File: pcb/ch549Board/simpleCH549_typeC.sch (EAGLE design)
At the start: 14 parts, among them J4 USB_A_SMT_MALE, U2 CH552G

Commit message: update pins in text editor
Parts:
- LED2: value P3.3 -> P2.2
- U2: value CH552G -> CH549G; device myOwnLib:MY_IC_CH551G_CH552GSOP-16 -> myOwnLib:MY_IC_CH549GSOP-16
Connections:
- removed net P3.2: J2.5, U2.P3.2
- removed net P3.3: J2.6, R3.1, U2.P3.3
- new net P2.2: J2.6, R3.1, U2.P2.2
- new net P2.4: J2.7, U2.P2.4
- net P1.1: now also J2.5; no longer J1.2
- net P3.0: now also J2.4; no longer J2.3
- net P3.1: now also J2.3; no longer J2.4
- net P3.4: now also J1.2; no longer J2.7
- net USB_D+: now also U2.P5.1; no longer U2.P3.6
- net USB_D-: now also U2.P5.0; no longer U2.P3.7
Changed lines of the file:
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@@
 <part name="GND3" library="SparkFun-PowerSymbols" library_urn="urn:adsk.eagle:library:530" deviceset="GND" device=""/>
 <part name="R2" library="rcl" library_urn="urn:adsk.eagle:library:334" deviceset="R-US_" device="R0805" package3d_urn="urn:adsk.eagle:package:23553/2" value="20K"/>
-<part name="U2" library="myOwnLib" deviceset="MY_IC_CH551G_CH552G" device="SOP-16" value="CH552G">
+<part name="U2" library="myOwnLib" deviceset="MY_IC_CH549G" device="SOP-16" value="CH549G">
 <attribute name="LCSC" value="C111292"/>
 </part>
@@
 <part name="S1" library="SparkFun-Switches" library_urn="urn:adsk.eagle:library:535" deviceset="MOMENTARY-SWITCH-SPST" device="-SMD-6.2MM-TALL" package3d_urn="urn:adsk.eagle:package:40172/1"/>
 <part name="R3" library="rcl" library_urn="urn:adsk.eagle:library:334" deviceset="R-US_" device="R0805" package3d_urn="urn:adsk.eagle:package:23553/2" value="20K"/>
-<part name="LED2" library="BeagleBone_Black_Wireless" library_urn="urn:adsk.eagle:library:6644236" deviceset="GHI-BASICCOMPONENTS_LED-(INCH)-" device="0805" package3d_urn="urn:adsk.eagle:package:6644356/2" value="P3.3"/>
+<part name="LED2" library="BeagleBone_Black_Wireless" library_urn="urn:adsk.eagle:library:6644236" deviceset="GHI-BASICCOMPONENTS_LED-(INCH)-" device="0805" package3d_urn="urn:adsk.eagle:package:6644356/2" value="P2.2"/>
 <part name="GND6" library="SparkFun-PowerSymbols" library_urn="urn:adsk.eagle:library:530" deviceset="GND" device=""/>
 <part name="GOLD_ORB_SM1" library="oshw" deviceset="OSHWLOGO" device="LOGO8MM"/>
@@
 <wire x1="127" y1="25.4" x2="134.62" y2="25.4" width="0.1524" layer="91"/>
 <label x="127" y="25.4" size="1.778" layer="95"/>
-<pinref part="U2" gate="G$1" pin="P3.7"/>
+<pinref part="U2" gate="G$1" pin="P5.0"/>
 </segment>
 </net>
@@
 <wire x1="127" y1="22.86" x2="134.62" y2="22.86" width="0.1524" layer="91"/>
 <label x="127" y="22.86" size="1.778" layer="95"/>
-<pinref part="U2" gate="G$1" pin="P3.6"/>
+<pinref part="U2" gate="G$1" pin="P5.1"/>
 </segment>
 <segment>
@@
 </segment>
 </net>
-<net name="P1.1" class="0">
+<net name="P3.4" class="0">
 <segment>
 <label x="127" y="30.48" size="1.778" layer="95"/>
 <wire x1="133.35" y1="30.48" x2="127" y2="30.48" width="0.1524" layer="91"/>
-<pinref part="U2" gate="G$1" pin="P1.1"/>
+<pinref part="U2" gate="G$1" pin="P3.4"/>
 </segment>
 <segment>
@@
 </segment>
 </net>
-<net name="P3.4" class="0">
+<net name="P2.4" class="0">
 <segment>
 <wire x1="127" y1="20.32" x2="134.62" y2="20.32" width="0.1524" layer="91"/>
 <label x="127" y="20.32" size="1.778" layer="95"/>
-<pinref part="U2" gate="G$1" pin="P3.4"/>
+<pinref part="U2" gate="G$1" pin="P2.4"/>
 </segment>
 <segment>
@@
 </segment>
 </net>
-<net name="P3.3" class="0">
+<net name="P2.2" class="0">
 <segment>
 <label x="127" y="17.78" size="1.778" layer="95"/>
 <wire x1="127" y1="17.78" x2="134.62" y2="17.78" width="0.1524" layer="91"/>
-<pinref part="U2" gate="G$1" pin="P3.3"/>
+<pinref part="U2" gate="G$1" pin="P2.2"/>
 <pinref part="R3" gate="G$1" pin="1"/>
 </segment>
@@
 </segment>
 </net>
-<net name="P3.2" class="0">
+<net name="P1.1" class="0">
 <segment>
 <wire x1="127" y1="15.24" x2="134.62" y2="15.24" width="0.1524" layer="91"/>
 <label x="127" y="15.24" size="1.778" layer="95"/>
-<pinref part="U2" gate="G$1" pin="P3.2"/>
+<pinref part="U2" gate="G$1" pin="P1.1"/>
 </segment>
 <segment>
@@
 </segment>
 </net>
-<net name="P3.1" class="0">
+<net name="P3.0" class="0">
 <segment>
 <label x="127" y="12.7" size="1.778" layer="95"/>
 <wire x1="127" y1="12.7" x2="134.62" y2="12.7" width="0.1524" layer="91"/>
-<pinref part="U2" gate="G$1" pin="P3.1"/>
+<pinref part="U2" gate="G$1" pin="P3.0"/>
 </segment>
 <segment>
@@
 </segment>
 </net>
-<net name="P3.0" class="0">
+<net name="P3.1" class="0">
 <segment>
 <label x="127" y="10.16" size="1.778" layer="95"/>
 <wire x1="127" y1="10.16" x2="134.62" y2="10.16" width="0.1524" layer="91"/>
-<pinref part="U2" gate="G$1" pin="P3.0"/>
-</segment>
-<segment>
+<pinref part="U2" gate="G$1" pin="P3.1"/>
+</segment>
+<segment>

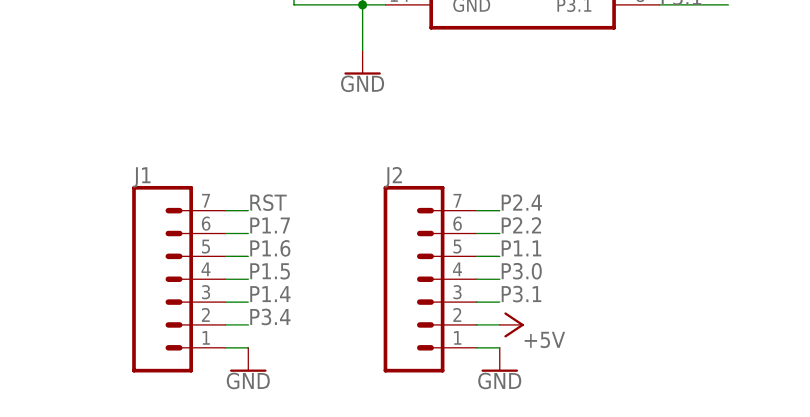
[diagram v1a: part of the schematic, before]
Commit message: adjust pins
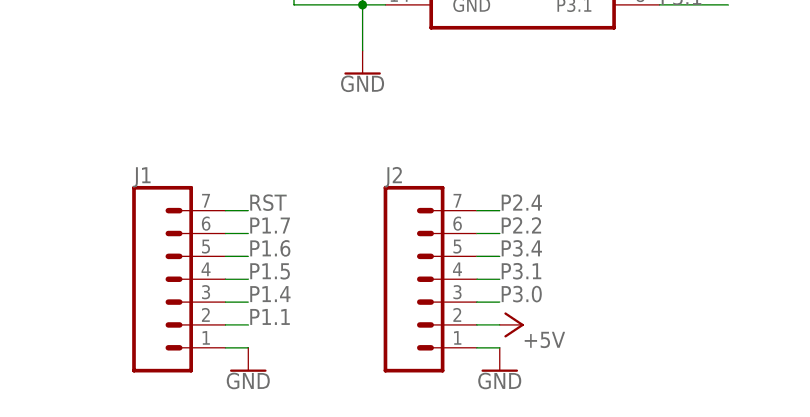
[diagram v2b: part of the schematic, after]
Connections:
- net P1.1: now also J1.2; no longer J2.5
- net P3.0: now also J2.3; no longer J2.4
- net P3.1: now also J2.4; no longer J2.3
- net P3.4: now also J2.5; no longer J1.2
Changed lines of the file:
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@@
 </segment>
 <segment>
-<pinref part="J1" gate="G$1" pin="2"/>
-<wire x1="78.74" y1="-25.4" x2="81.28" y2="-25.4" width="0.1524" layer="91"/>
-<label x="81.28" y="-25.4" size="1.778" layer="95"/>
+<pinref part="J2" gate="G$1" pin="5"/>
+<wire x1="106.68" y1="-17.78" x2="109.22" y2="-17.78" width="0.1524" layer="91"/>
+<label x="109.22" y="-17.78" size="1.778" layer="95"/>
 </segment>
 </net>
@@
 </segment>
 <segment>
-<pinref part="J2" gate="G$1" pin="5"/>
-<wire x1="106.68" y1="-17.78" x2="109.22" y2="-17.78" width="0.1524" layer="91"/>
-<label x="109.22" y="-17.78" size="1.778" layer="95"/>
-</segment>
-</net>
-<net name="P3.0" class="0">
-<segment>
-<label x="127" y="12.7" size="1.778" layer="95"/>
-<wire x1="127" y1="12.7" x2="134.62" y2="12.7" width="0.1524" layer="91"/>
-<pinref part="U2" gate="G$1" pin="P3.0"/>
-</segment>
-<segment>
-<pinref part="J2" gate="G$1" pin="4"/>
-<wire x1="106.68" y1="-20.32" x2="109.22" y2="-20.32" width="0.1524" layer="91"/>
-<label x="109.22" y="-20.32" size="1.778" layer="95"/>
-</segment>
-</net>
-<net name="P3.1" class="0">
-<segment>
-<label x="127" y="10.16" size="1.778" layer="95"/>
-<wire x1="127" y1="10.16" x2="134.62" y2="10.16" width="0.1524" layer="91"/>
-<pinref part="U2" gate="G$1" pin="P3.1"/>
-</segment>
-<segment>
-<pinref part="J2" gate="G$1" pin="3"/>
-<wire x1="106.68" y1="-22.86" x2="109.22" y2="-22.86" width="0.1524" layer="91"/>
-<label x="109.22" y="-22.86" size="1.778" layer="95"/>
+<pinref part="J1" gate="G$1" pin="2"/>
+<wire x1="78.74" y1="-25.4" x2="81.28" y2="-25.4" width="0.1524" layer="91"/>
+<label x="81.28" y="-25.4" size="1.778" layer="95"/>
 </segment>
 </net>
@@
 </segment>
 </net>
+<net name="P3.0" class="0">
+<segment>
+<pinref part="J2" gate="G$1" pin="3"/>
+<wire x1="106.68" y1="-22.86" x2="109.22" y2="-22.86" width="0.1524" layer="91"/>
+<label x="109.22" y="-22.86" size="1.778" layer="95"/>
+</segment>
+<segment>
+<label x="127" y="12.7" size="1.778" layer="95"/>
+<wire x1="127" y1="12.7" x2="134.62" y2="12.7" width="0.1524" layer="91"/>
+<pinref part="U2" gate="G$1" pin="P3.0"/>
+</segment>
+</net>
+<net name="P3.1" class="0">
+<segment>
+<label x="127" y="10.16" size="1.778" layer="95"/>
+<wire x1="127" y1="10.16" x2="134.62" y2="10.16" width="0.1524" layer="91"/>
+<pinref part="U2" gate="G$1" pin="P3.1"/>
+</segment>
+<segment>
+<pinref part="J2" gate="G$1" pin="4"/>
+<wire x1="106.68" y1="-20.32" x2="109.22" y2="-20.32" width="0.1524" layer="91"/>
+<label x="109.22" y="-20.32" size="1.778" layer="95"/>
+</segment>
+</net>

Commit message: update board
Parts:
- removed F1: (no value), adafruit:PTCFUSE-1206
- added C3: 0.1uF, rcl:C-EUC0805K
- added J3: 629722000214, Wurth_Connectors_WR-USB:629722000214
- added U1: MCP1703CB, linear:MCP1703CB
- J4: value USB_A_SMT_MALE -> (none); device SparkFun-Connectors:USB_A_SMT_MALE -> SparkFun-Connectors:CONN_021X02_NO_SILK
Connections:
- new net VUSB: C3.1, J3.VBUS, J3.VBUS1, J3.VBUS2, J3.VBUS3, J4.2, U1.VI
- net +5V: now also U1.VO; no longer F1.1, F1.2, J4.VBUS
- net GND: now also C3.2, J3.GND, J3.GND1, J3.GND2, J3.GND3, J4.1, U1.GND; no longer J4.GND
- net P1.4: now also J3.CC1
- net P1.5: now also J3.CC2
- net USB_D+: now also J3.D+1, J3.D+2; no longer J4.D+
- net USB_D-: now also J3.D-1, J3.D-2; no longer J4.D-

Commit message: board finish
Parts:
- added J5: (no value), SparkFun-Connectors:CONN_021X02_NO_SILK
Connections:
- net GND: now also J5.1
- net VUSB: now also J5.2
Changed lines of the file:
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@@
 <part name="J4" library="SparkFun-Connectors" library_urn="urn:adsk.eagle:library:513" deviceset="CONN_02" device="1X02_NO_SILK" package3d_urn="urn:adsk.eagle:package:38051/1"/>
 <part name="GND7" library="SparkFun-PowerSymbols" library_urn="urn:adsk.eagle:library:530" deviceset="GND" device=""/>
+<part name="J5" library="SparkFun-Connectors" library_urn="urn:adsk.eagle:library:513" deviceset="CONN_02" device="1X02_NO_SILK" package3d_urn="urn:adsk.eagle:package:38051/1"/>
+<part name="GND8" library="SparkFun-PowerSymbols" library_urn="urn:adsk.eagle:library:530" deviceset="GND" device=""/>
 </parts>
 <sheets>
@@
 <attribute name="VALUE" x="132.08" y="-20.574" size="1.778" layer="96" align="top-center"/>
 </instance>
+<instance part="J5" gate="G$1" x="139.7" y="-15.24" smashed="yes">
+<attribute name="VALUE" x="137.16" y="-20.066" size="1.778" layer="96" font="vector"/>
+<attribute name="NAME" x="139.7" y="-9.652" size="1.778" layer="95" font="vector"/>
+</instance>
+<instance part="GND8" gate="1" x="147.32" y="-20.32" smashed="yes">
+<attribute name="VALUE" x="147.32" y="-20.574" size="1.778" layer="96" align="top-center"/>
+</instance>
 </instances>
 <busses>
@@
 <wire x1="132.08" y1="-15.24" x2="132.08" y2="-17.78" width="0.1524" layer="91"/>
 </segment>
+<segment>
+<pinref part="J5" gate="G$1" pin="1"/>
+<pinref part="GND8" gate="1" pin="GND"/>
+<wire x1="147.32" y1="-15.24" x2="147.32" y2="-17.78" width="0.1524" layer="91"/>
+</segment>
 </net>
 <net name="3.3V" class="0">
@@
 <label x="132.08" y="-10.16" size="1.778" layer="95"/>
 </segment>
-</net>
+<segment>
+<pinref part="J5" gate="G$1" pin="2"/>
+<wire x1="147.32" y1="-12.7" x2="147.32" y2="-10.16" width="0.1524" layer="91"/>
+<label x="147.32" y="-10.16" size="1.778" layer="95"/>
+</segment>
+</net>
